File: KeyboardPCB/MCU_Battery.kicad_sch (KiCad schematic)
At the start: 41 parts, among them Q1 CSD17527Q5A, Q2 CSD17527Q5A, U1 ATmega32U4-M, U2 TPS61236PRWLT, U3 BQ297xy, U4 BQ24193RGER, Y1 ECS-160-7-33B-CKL-TR

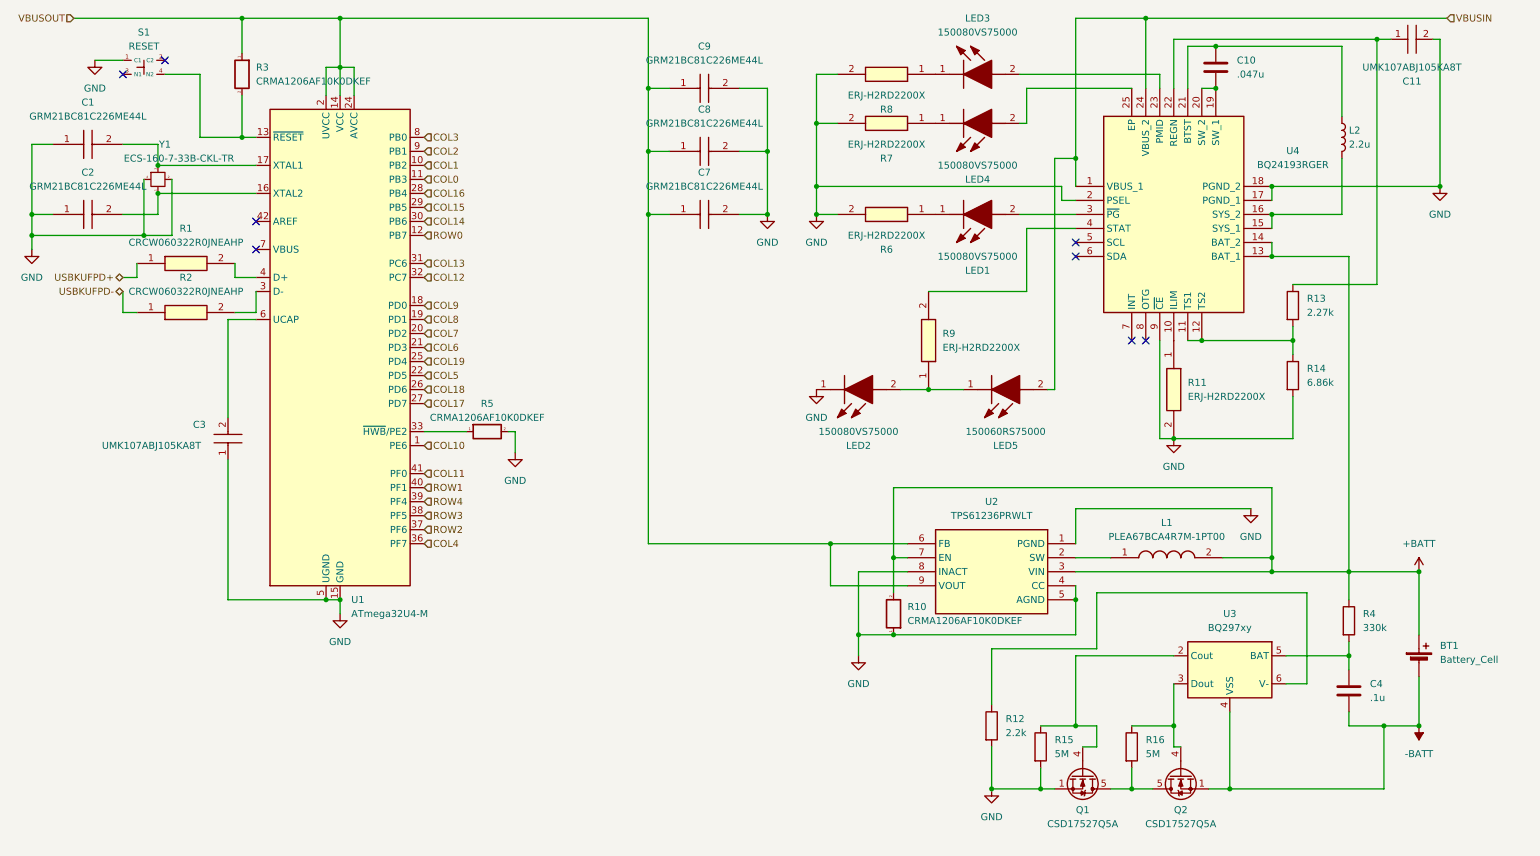
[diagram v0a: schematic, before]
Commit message: populated Keyboard
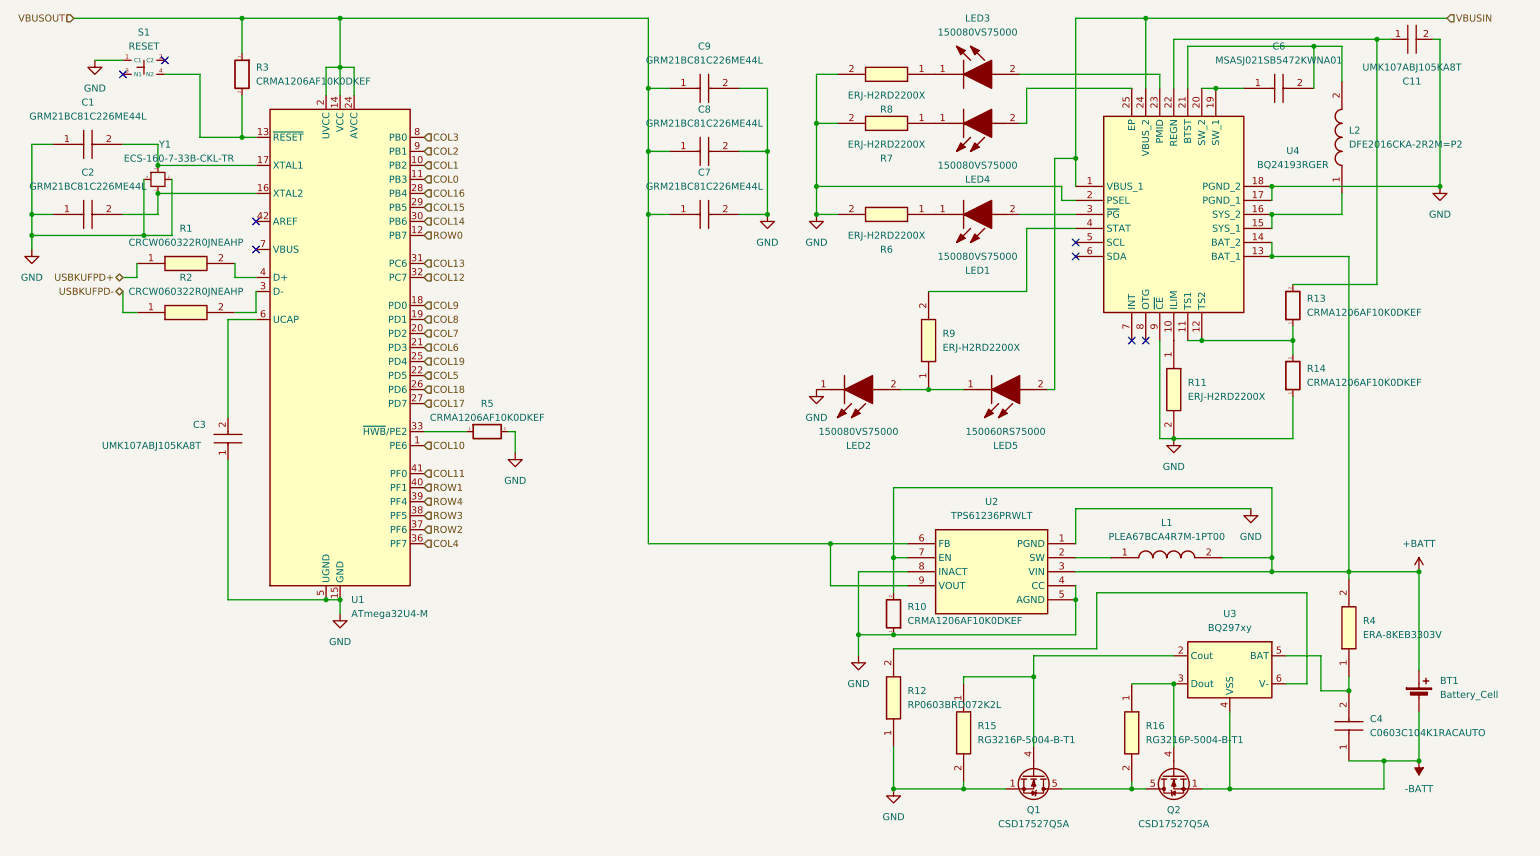
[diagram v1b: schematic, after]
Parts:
- removed C10: .047u, symbol Device:C
- removed C4: .1u, symbol Device:C
- removed L2: 2.2u, symbol Device:L
- removed R12: 2.2k, symbol Device:R
- removed R13: 2.27k, symbol Device:R
- removed R14: 6.86k, symbol Device:R
- removed R15, R16: 5M, symbol Device:R
- removed R4: 330k, symbol Device:R
- added C4: C0603C104K1RACAUTO, keyboard_syms:CAPC1608X95N, symbol keyboard_syms:C0603C104K1RACAUTO
- added C6: MSASJ021SB5472KWNA01, keyboard_syms:CAPC0201X14N, symbol keyboard_syms:MSASJ021SB5472KWNA01
- added L2: DFE2016CKA-2R2M=P2, keyboard_syms:DFE2016CKA1R0MP2, symbol keyboard_syms:DFE2016CKA-2R2M=P2
- added R12: RP0603BRD072K2L, keyboard_syms:RESC1608X55N, symbol keyboard_syms:RP0603BRD072K2L
- added R13, R14: CRMA1206AF10K0DKEF, keyboard_syms:RESC3216X74N, symbol keyboard_syms:CRMA1206AF10K0DKEF
- added R15, R16: RG3216P-5004-B-T1, keyboard_syms:RESC3216X50N, symbol keyboard_syms:RG3216P-5004-B-T1
- added R4: ERA-8KEB3303V, keyboard_syms:ERA8KEB1004V, symbol keyboard_syms:ERA-8KEB3303V
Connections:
- net +BATT: now also R4.2
- net -BATT: now also C4.1
- net GND: now also R12.1, R14.1, R15.2
- net at Q2.4 (G), U3.3 (Dout): now also R16.1
- net at Q1.5 (D), Q2.5 (D): now also R16.2
- net at U4.11 (TS1), U4.12 (TS2): now also R13.1, R14.2
- net at Q1.4 (G), U3.2 (Cout): now also R15.1
- net at C11.1, U4.22 (REGN): now also R13.2
- net at U3.5 (BAT): now also C4.2, R4.1
- net at U3.6 (V-): now also R12.2
- net at U4.21 (BTST): now also C6.2, L2.2
- net at U4.19 (SW_1), U4.20 (SW_2): now also C6.1
- net at U4.15 (SYS_1), U4.16 (SYS_2): now also L2.1
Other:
- moved on the sheet: BT1, Q1, Q2

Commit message: Began routing PCB
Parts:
- removed BT1: Battery_Cell, symbol Device:Battery_Cell
- added BT1: Battery_Cell_JST-PH, Connector_JST:JST_PH_B2B-PH-K_1x02_P2.00mm_Vertical, symbol keyboard_syms:Battery_Cell_JST-PH
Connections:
- net +BATT: now also BT1.1 (+)
- net -BATT: now also BT1.2 (-)
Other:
- moved on the sheet: C4, L1, Q1, Q2, R10, R12, R15, R16, R4, U2, U3

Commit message: Finalised schematic, progress on board layout
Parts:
- renumbered C11 to C10, C1 to C2, C2 to C3, C3 to C4, C9 to C5, C8 to C6, C6 to C8, C4 to C9, LED2 to LED1, LED3 to LED2, LED4 to LED3, LED1 to LED4, R15 to R10, R9 to R11, R16 to R12, R11 to R13, R13 to R14, R14 to R15, R4 to R16, R5 to R4, R10 to R5, R12 to R6, R8 to R7, R7 to R8, R6 to R9, U4 to U3, U3 to U4

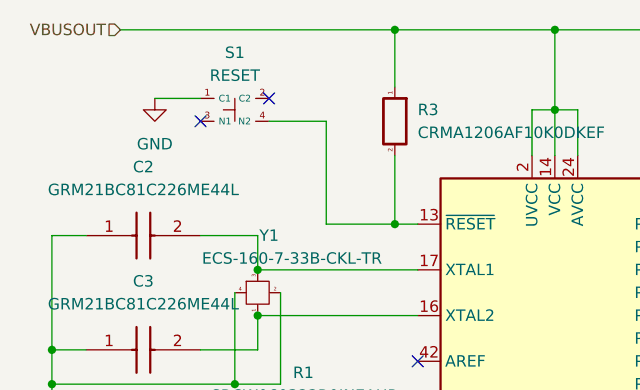
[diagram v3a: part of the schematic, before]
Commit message: Reorganised backside
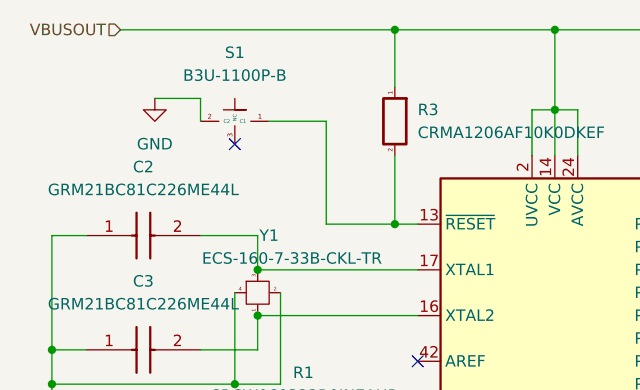
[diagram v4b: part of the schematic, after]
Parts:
- removed S1: RESET, keyboard_syms:B3FS1012P, symbol keyboard_syms:B3FS-1012P
- added S1: B3U-1100P-B, keyboard_syms:B3U1100PB, symbol keyboard_syms:B3U-1100P-B
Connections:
- net GND: now also S1.2 (C2)
- net at R3.2, U1.13 (~{RESET}): now also S1.1 (C1)
- no-connect marks 8 -> 7
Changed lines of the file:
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@@
   )
   (no_connect (at 58.42 52.07))
-  (no_connect (at 34.29 25.4))
   (no_connect (at 207.01 55.88))
-  (no_connect (at 41.91 22.86))
   (no_connect (at 217.17 73.66))
   (no_connect (at 207.01 58.42))
+  (no_connect (at 38.1 27.94))
   (no_connect (at 58.42 57.15))
   (no_connect (at 219.71 73.66))
@@
   )
   (wire (pts (xy 73.66 120.65) (xy 73.66 123.19))
+    (stroke (width 0) (type default))
+  )
+  (wire (pts (xy 34.29 22.86) (xy 34.29 25.4))
     (stroke (width 0) (type default))
   )
@@
     )
   )
-  (symbol (lib_id "keyboard_syms:B3FS-1012P") (at 38.1 24.13 0) (unit 1)
-    (in_bom yes) (on_board yes) (dnp no)
-    (property "Reference" "S1" (at 38.1 17.78 0)
-      (effects (font (size 1.27 1.27)))
-    )
-    (property "Value" "RESET" (at 38.1 20.32 0)
-      (effects (font (size 1.27 1.27)))
-    )
-    (property "Footprint" "keyboard_syms:B3FS1012P" (at 64.77 119.05 0)
-      (effects (font (size 1.27 1.27)) (justify left top) hide)
-    )
-    (property "Datasheet" "https://omronfs.omron.com/en_US/ecb/products/pdf/en-b3fs.pdf" (at 64.77 219.05 0)
-      (effects (font (size 1.27 1.27)) (justify left top) hide)
-    )
-    (property "Description" "Tactile Switches 5 x 5 mm, 2.5 mm Actuator Height, 160 gf, Silver, Surface Mount, TR, SPST, Tactile Switch" (at 64.77 26.67 0)
-      (effects (font (size 1.27 1.27)) (justify left) hide)
-    )
-    (property "Height" "4.3" (at 64.77 419.05 0)
-      (effects (font (size 1.27 1.27)) (justify left top) hide)
-    )
-    (property "Manufacturer_Name" "Omron Electronics" (at 64.77 519.05 0)
-      (effects (font (size 1.27 1.27)) (justify left top) hide)
-    )
-    (property "Manufacturer_Part_Number" "B3FS-1012P" (at 64.77 619.05 0)
-      (effects (font (size 1.27 1.27)) (justify left top) hide)
-    )
-    (property "Mouser Part Number" "653-B3FS-1012P" (at 64.77 719.05 0)
-      (effects (font (size 1.27 1.27)) (justify left top) hide)
-    )
-    (property "Mouser Price/Stock" "https://www.mouser.co.uk/ProductDetail/Omron-Electronics/B3FS-1012P?qs=1tDaWCEHQQ7mwfTJVAKWQA%3D%3D" (at 64.77 819.05 0)
-      (effects (font (size 1.27 1.27)) (justify left top) hide)
-    )
-    (property "Arrow Part Number" "B3FS-1012P" (at 64.77 919.05 0)
-      (effects (font (size 1.27 1.27)) (justify left top) hide)
-    )
-    (property "Arrow Price/Stock" "https://www.arrow.com/en/products/b3fs-1012p/omron?region=nac" (at 64.77 1019.05 0)
-      (effects (font (size 1.27 1.27)) (justify left top) hide)
-    )
-    (property "Mouser Testing Part Number" "" (at 64.77 46.99 0)
-      (effects (font (size 1.27 1.27)) (justify left) hide)
-    )
-    (property "Mouser Testing Price/Stock" "" (at 64.77 49.53 0)
-      (effects (font (size 1.27 1.27)) (justify left) hide)
-    )
-    (pin "1")
-    (pin "2")
-    (pin "3")
-    (pin "4")
-    (instances
-      (project "KeyboardPCB"
-        (path "/0ddec2b6-b97f-44d3-913e-9f8ffaa22885/0e04ce72-6533-49cc-b4b5-6fa7ba1a6887"
-          (reference "S1") (unit 1)
-        )
-      )
-    )
-  )
   (symbol (lib_id "keyboard_syms:CRMA1206AF10K0DKEF") (at 55.88 25.4 270) (unit 1)
     (in_bom yes) (on_board yes) (dnp no)
@@
         )
       )
+    )
+  )
+  (symbol (lib_id "keyboard_syms:B3U-1100P-B") (at 38.1 25.4 0) (unit 1)
+    (in_bom yes) (on_board yes) (dnp no) (fields_autoplaced)
+    (property "Reference" "S1" (at 38.1 17.78 0)
+      (effects (font (size 1.27 1.27)))
+    )
+    (property "Value" "B3U-1100P-B" (at 38.1 20.32 0)
+      (effects (font (size 1.27 1.27)))
+    )
+    (property "Footprint" "keyboard_syms:B3U1100PB" (at 72.39 120.32 0)
+      (effects (font (size 1.27 1.27)) (justify left top) hide)
+    )
+    (property "Datasheet" "https://omronfs.omron.com/en_US/ecb/products/pdf/en-b3u.pdf" (at 72.39 220.32 0)
+      (effects (font (size 1.27 1.27)) (justify left top) hide)
+    )
+    (property "Height" "1.75" (at 72.39 420.32 0)
+      (effects (font (size 1.27 1.27)) (justify left top) hide)
+    )
+    (property "Manufacturer_Name" "Omron Electronics" (at 72.39 520.32 0)
+      (effects (font (size 1.27 1.27)) (justify left top) hide)
+    )
+    (property "Manufacturer_Part_Number" "B3U-1100P-B" (at 72.39 620.32 0)
+      (effects (font (size 1.27 1.27)) (justify left top) hide)
+    )
+    (property "Mouser Part Number" "653-B3U-1100P-B" (at 72.39 720.32 0)
+      (effects (font (size 1.27 1.27)) (justify left top) hide)
+    )
+    (property "Mouser Price/Stock" "https://www.mouser.co.uk/ProductDetail/Omron-Electronics/B3U-1100P-B?qs=q8ECNkb1%2FvOX21F1CoxJgQ%3D%3D" (at 72.39 820.32 0)
+      (effects (font (size 1.27 1.27)) (justify left top) hide)
+    )
+    (property "Arrow Part Number" "B3U-1100P-B" (at 72.39 920.32 0)
+      (effects (font (size 1.27 1.27)) (justify left top) hide)
+    )
+    (property "Arrow Price/Stock" "https://www.arrow.com/en/products/b3u-1100p-b/omron?region=nac" (at 72.39 1020.32 0)
+      (effects (font (size 1.27 1.27)) (justify left top) hide)
+    )
+    (pin "1")
+    (pin "2")
+    (pin "3")
+    (instances
+      (project "KeyboardPCB"
+        (path "/0ddec2b6-b97f-44d3-913e-9f8ffaa22885/0e04ce72-6533-49cc-b4b5-6fa7ba1a6887"
+          (reference "S1") (unit 1)
+        )
+      )
